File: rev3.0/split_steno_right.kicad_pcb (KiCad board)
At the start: 2 copper layers, 99.7 x 74.2 mm, 44 parts, among them J1 USB_B, J2 Audio-Jack-4, J3 Conn_02x04_Odd_Even, J4 Conn_01x03, J5 Conn_01x03, J6 Conn_01x02, M2 MountingHole_2.2mm_M2, P1 TC2030-IDC, SW1 SW_Push, SW10 SW_Push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

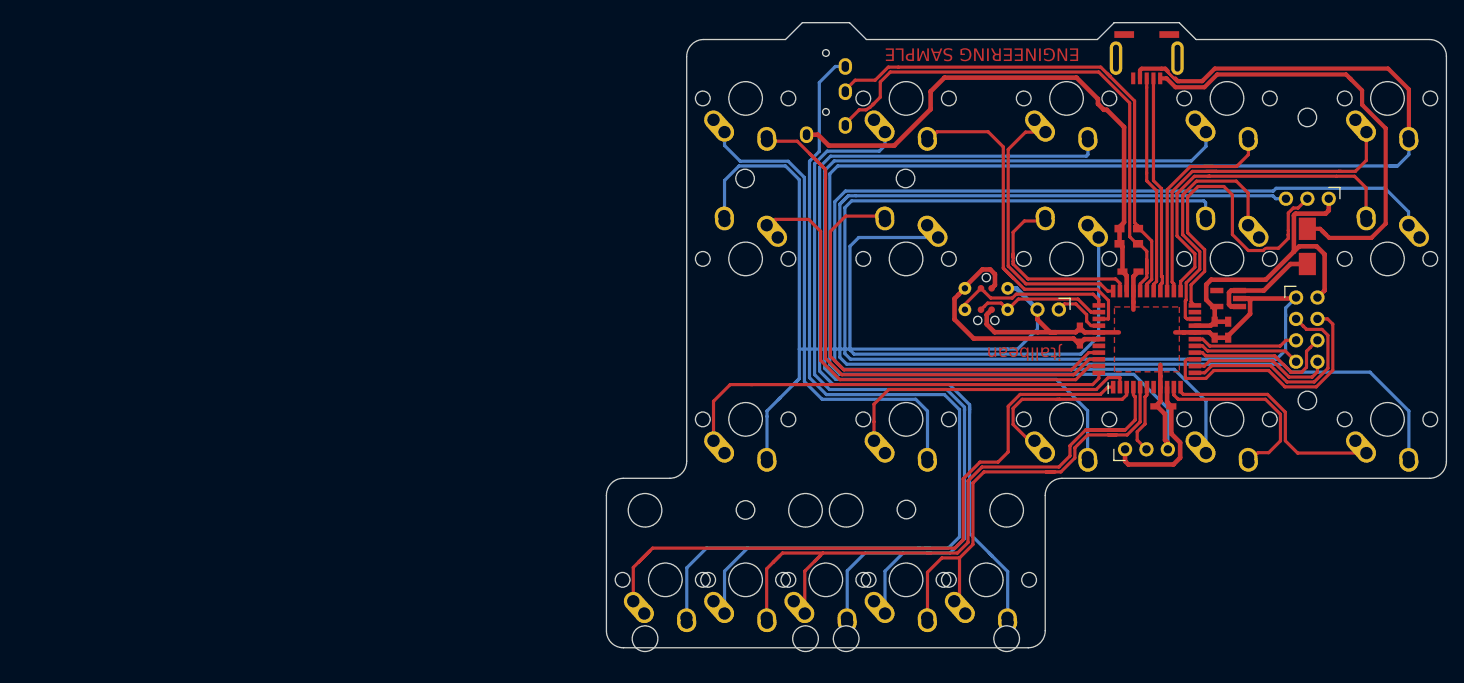
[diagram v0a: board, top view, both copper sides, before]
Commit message: flipped x values
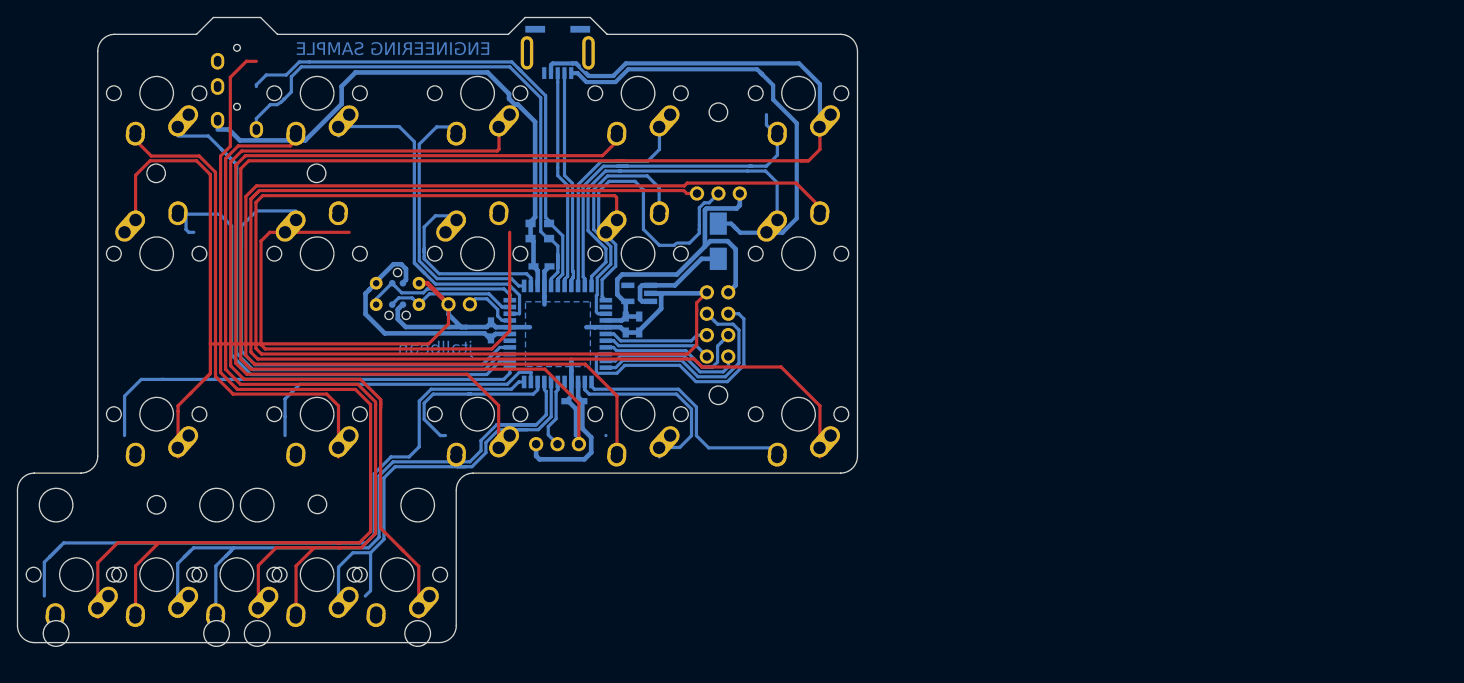
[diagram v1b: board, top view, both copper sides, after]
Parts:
- C1, C2, C3, C4, C5, F1, G***, J1, J2, J3, J4, J5, J6, P1, R1, R2, U1, U2: moved to B.Cu
- M2 (x6), SW1, SW10, SW11, SW12, SW13, SW14, SW15, SW16, SW17, SW18, SW19, SW2, SW20, SW3, SW4, SW5, SW6, SW7, SW8, SW9: moved to F.Cu
- moved J3 70.3 mm to (115.4, 75.2)
- moved U2 69.9 mm to (97.7, 72.5)
- moved F1 69.9 mm to (116.7, 61.5), turned to 270 degrees
- moved J1 69.9 mm to (97.7, 41.5), turned to 0 degrees
- moved M2 69.9 mm to (50.0, 92.8), turned to 0 degrees
- moved M2 69.9 mm to (69.0, 53.4), turned to 0 degrees
- moved R1 69.9 mm to (95.5, 61.1), turned to 0 degrees
- moved R2 69.9 mm to (95.5, 59.4), turned to 0 degrees
- moved SW1 69.9 mm to (126.3, 43.9), turned to 180 degrees
- moved SW11 69.9 mm to (126.3, 82.0), turned to 180 degrees
- moved SW14 69.9 mm to (69.1, 82.0), turned to 180 degrees
- moved SW16 69.9 mm to (78.6, 101.0), turned to 180 degrees
- moved SW19 69.9 mm to (69.1, 101.0), turned to 180 degrees
- moved SW4 69.9 mm to (69.1, 43.9), turned to 180 degrees
- moved SW6 69.9 mm to (126.3, 62.9), turned to 0 degrees
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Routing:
- net GND: track 1315.3 -> 1147.6 mm
- net /KEY7: track 30.1 -> 149.5 mm
- net /KEY3: track 33.1 -> 109.4 mm
- net /KEY11: track 27.6 -> 101.2 mm
- net /KEY18: track 79.2 -> 7.50 mm
- net /KEY1: track 43.4 -> 113.1 mm
- net (no net): track 0.00 -> 65.5 mm
- net /KEY17: track 80.6 -> 16.3 mm
- net Net-(J1-Pad5): track 0.00 -> 43.1 mm
- net Net-(F1-Pad2): track 54.0 -> 11.0 mm
- net /KEY10: track 58.9 -> 17.1 mm
- net /EXTRA1: track 39.6 -> 3.18 mm
- net /KEY12: track 22.5 -> 56.9 mm
- net /KEY14: track 36.0 -> 7.72 mm
- net /CE: track 26.2 -> 53.7 mm
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- added copper zone on B.Cu, net GND
- removed copper zone on F.Cu, net GND
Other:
- outline, holes or cut-outs redrawn

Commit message: library managed
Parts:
- C1, C2, C3, C4, C5: footprint Capacitors_SMD:C_0603_HandSoldering -> lib_fp:C_0603_HandSoldering
- F1: footprint Fuse_Holders_and_Fuses:Fuse_SMD1206_HandSoldering -> lib_fp:Fuse_SMD1206_HandSoldering
- J1: footprint keyboard_parts:USB_miniB_hirose_5S8 -> lib_fp:USB_miniB_hirose_5S8
- J2: footprint Keebio-Parts:TRRS-PJ-320A -> lib_fp:TRRS-PJ-320A
- J3: footprint Pin_Headers:Pin_Header_Straight_2x04_Pitch2.54mm -> lib_fp:Pin_Header_Straight_2x04_Pitch2.54mm
- J4, J5: footprint Pin_Headers:Pin_Header_Straight_1x03_Pitch2.54mm -> lib_fp:Pin_Header_Straight_1x03_Pitch2.54mm
- J6: footprint Pin_Headers:Pin_Header_Straight_1x02_Pitch2.54mm -> lib_fp:Pin_Header_Straight_1x02_Pitch2.54mm
- P1: footprint Tag-Connect:TC2030-NL_SMALL_AND_IDC_PDI -> lib_fp:TC2030-NL_SMALL_AND_IDC_PDI
- R1, R2: footprint Resistors_SMD:R_0603_HandSoldering -> lib_fp:R_0603_HandSoldering
- SW1, SW10, SW11, SW12, SW13, SW14, SW15, SW16, SW17, SW18, SW2, SW3, SW4, SW5, SW6, SW7, SW8, SW9: footprint MX_Alps_Hybrid:MX-1U-NoLED -> lib_fp:MX-1U-NoLED
- SW19, SW20: footprint MX_Alps_Hybrid:MX-2U-NoLED -> lib_fp:MX-2U-NoLED
- U1: footprint TO_SOT_Packages_SMD:SOT-23-5_HandSoldering -> lib_fp:SOT-23-5_HandSoldering
- U2: footprint Housings_QFP:TQFP-44_10x10mm_Pitch0.8mm -> lib_fp:TQFP-44_10x10mm_Pitch0.8mm
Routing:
- net VCC: track 174.0 -> 341.8 mm
- net GND: track 1147.6 -> 997.3 mm
- net /KEY17: track 16.3 -> 127.7 mm
- net /SCL: track 58.7 -> 4.24 mm
- net /KEY9: track 41.1 -> 73.6 mm
- net /MOSI: track 34.8 -> 8.88 mm
- net Net-(U1-Pad4): track 23.3 -> 3.74 mm
- net /KEY16: track 48.7 -> 30.1 mm
- net /PDI: track 11.4 -> 23.1 mm
- net /KEY10: track 17.1 -> 6.84 mm
- net /RST: track 15.0 -> 5.31 mm
- net Net-(U2-Pad40): track 11.0 -> 1.76 mm
- net +5V: track 13.5 -> 22.4 mm
- net Net-(F1-Pad2): track 11.0 -> 2.01 mm
- net /KEY3: track 109.4 -> 117.3 mm
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
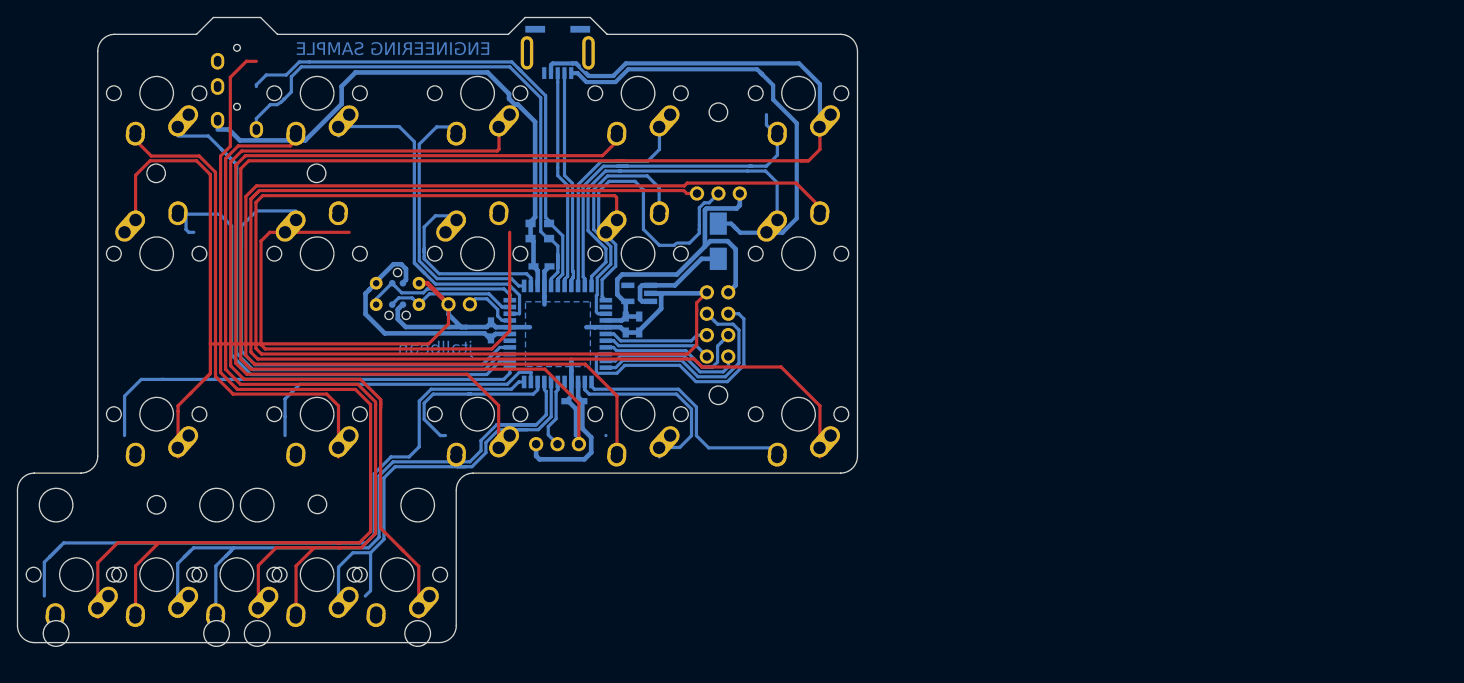
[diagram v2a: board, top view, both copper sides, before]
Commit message: filled gnd plane on left
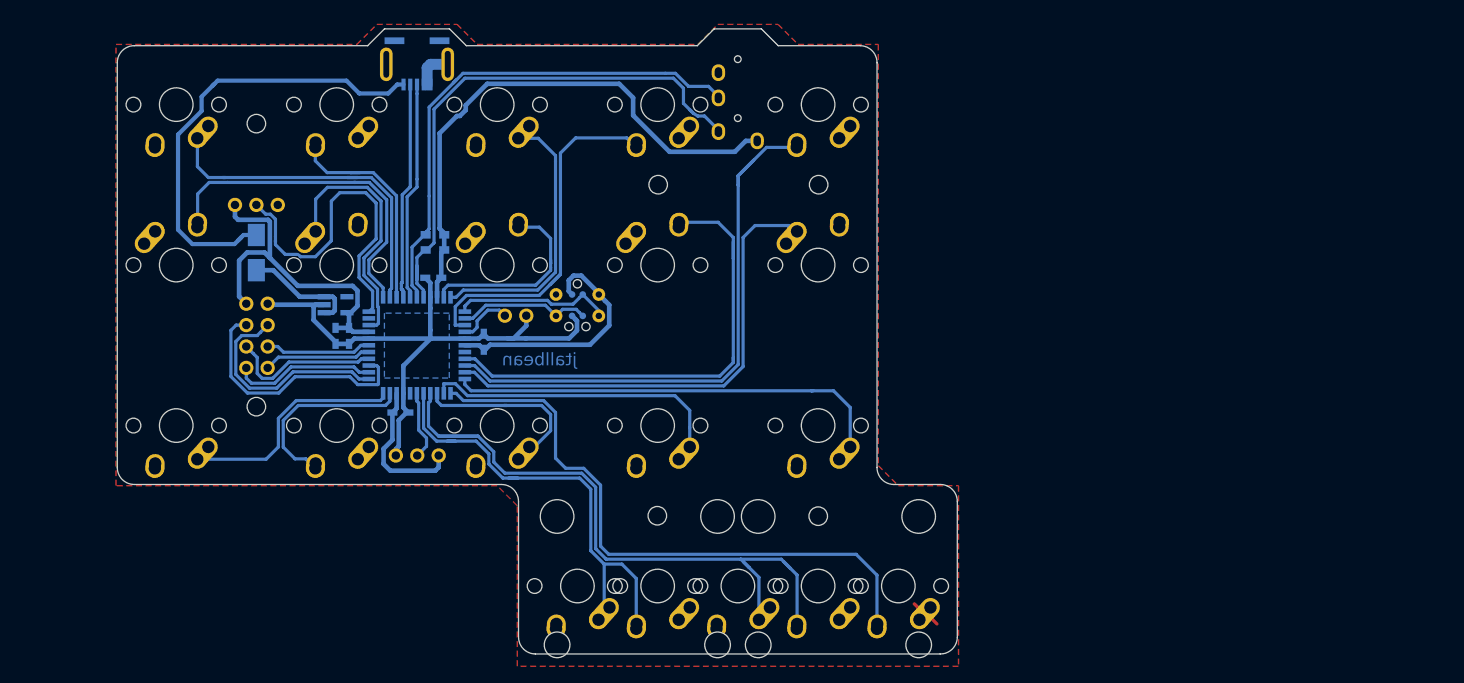
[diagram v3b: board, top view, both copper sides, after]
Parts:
- moved SW18 97.6 mm to (138.1, 102.4)
- moved M2 78.7 mm to (128.7, 54.8)
- moved M2 78.6 mm to (128.6, 94.1)
- moved SW10 78.5 mm to (128.6, 64.3)
- moved SW15 78.5 mm to (128.6, 83.3)
- moved SW20 78.5 mm to (128.6, 102.4)
- moved SW5 78.5 mm to (128.6, 45.2)
- moved SW1 73.9 mm to (52.4, 45.2)
- moved SW11 73.9 mm to (52.4, 83.3)
- moved SW6 73.9 mm to (52.4, 64.3)
- moved J5 59.9 mm to (59.4, 57.1), turned to 270 degrees
- moved SW17 59.5 mm to (119.1, 102.4)
- moved J2 59.5 mm to (119.0, 38.2)
- moved M2 54.9 mm to (61.9, 81.1)
- moved M2 54.9 mm to (61.9, 47.5)
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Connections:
- J1 pad 5: Net-(J1-Pad5) -> GND
- J1 pad 6: (no net) -> GND
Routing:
- net GND: track 997.3 -> 82.1 mm
- net VCC: track 341.8 -> 153.8 mm
- net /KEY7: track 152.2 -> 30.1 mm
- net /KEY3: track 117.3 -> 33.1 mm
- net /KEY1: track 119.8 -> 43.4 mm
- net /KEY11: track 101.2 -> 27.6 mm
- net /KEY18: track 7.50 -> 73.4 mm
- net (no net): track 65.5 -> 0.00 mm
- net /SCL: track 4.24 -> 64.6 mm
- net Net-(F1-Pad2): track 2.01 -> 54.0 mm
- net /KEY10: track 6.84 -> 58.9 mm
- net /KEY17: track 127.7 -> 80.6 mm
- net Net-(J1-Pad5): track 43.1 -> 0.00 mm
- net /EXTRA1: track 3.18 -> 39.6 mm
- net /KEY12: track 57.6 -> 22.5 mm
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- added copper zone on F.Cu, net GND
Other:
- outline, holes or cut-outs redrawn
- board text removed: "ENGINEERING SAMPLE"
